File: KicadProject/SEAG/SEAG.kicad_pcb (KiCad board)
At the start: 4 copper layers, 99.1 x 66.1 mm, 82 parts, among them J1 Screw_Terminal_01x02, J11 Screw_Terminal_01x02, J12 Screw_Terminal_01x02, J14 Screw_Terminal_01x08, J2 Conn_01x06_Pin, J3 Screw_Terminal_01x08, J4 Screw_Terminal_01x06, J5 Screw_Terminal_01x06, J6 Screw_Terminal_01x06, J7 Screw_Terminal_01x06, U1 STM32F722RCTx, Y1 Crystal_GND24

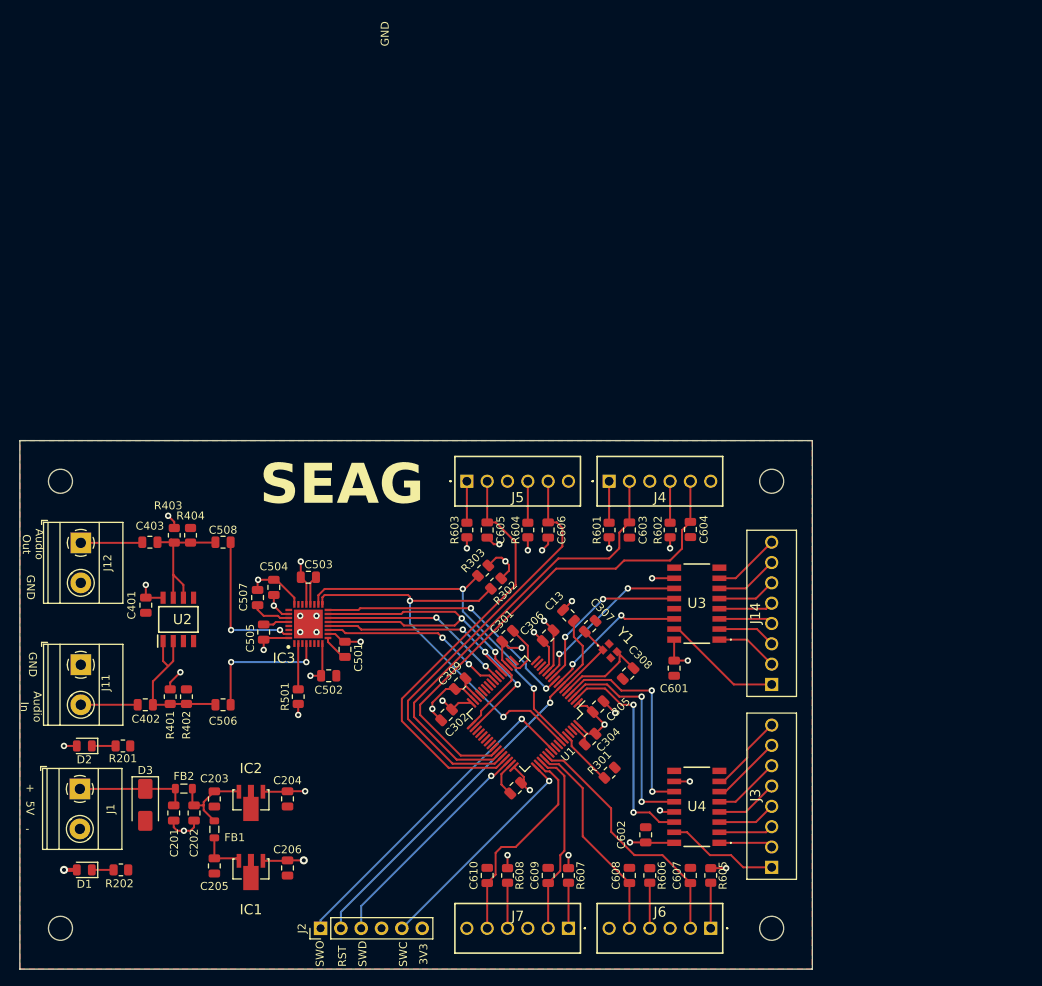
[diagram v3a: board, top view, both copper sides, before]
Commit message: Added rotary encoder screw terminal
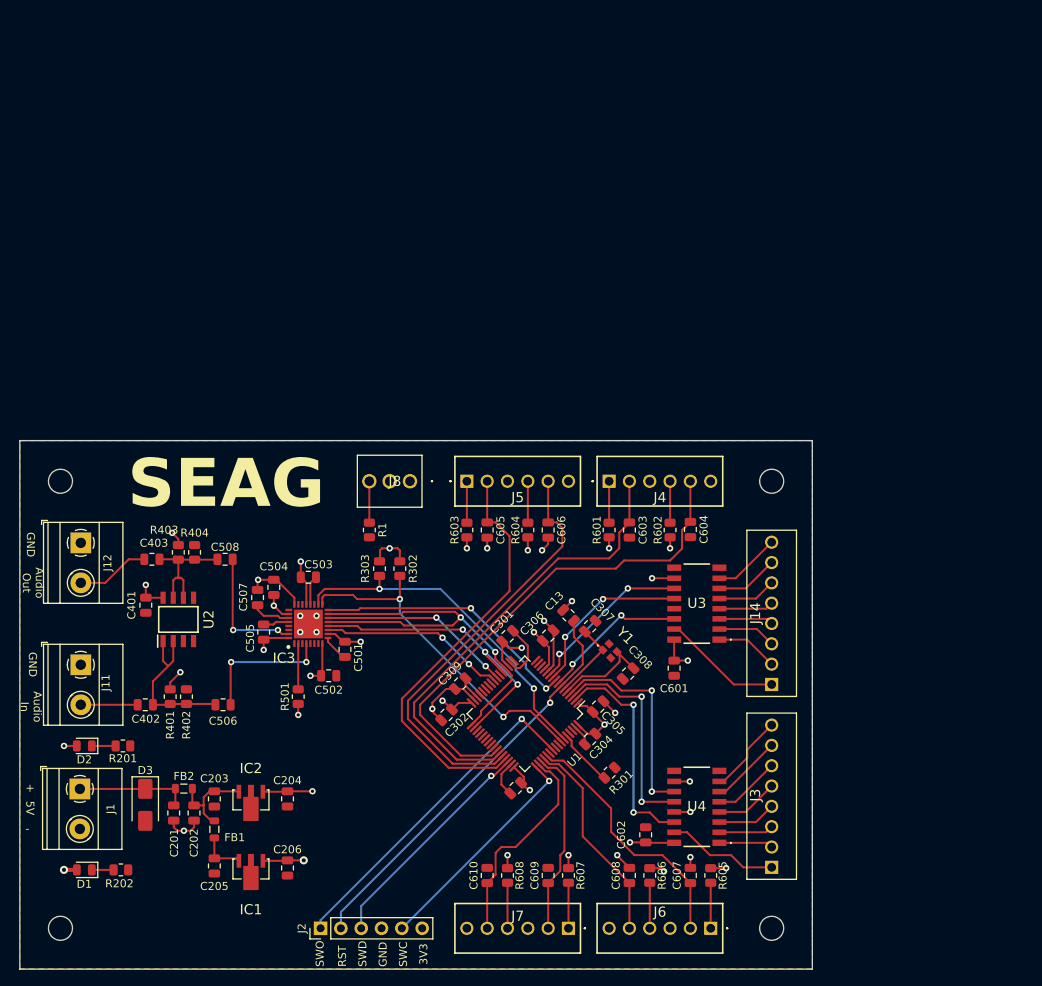
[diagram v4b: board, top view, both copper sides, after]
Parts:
- added J8: Screw_Terminal_01x03, SamacSys_Parts:2828343, F.Cu at (99.6, 91.4)
- added R1: 10K, Resistor_SMD:R_0805_2012Metric, F.Cu at (94.5, 97.5)
- moved R303 13.0 mm to (95.8, 102.4), turned to -90 degrees
- moved R302 12.2 mm to (98.3, 102.4), turned to -90 degrees
- moved R404 2.20 mm to (72.6, 100.3)
- moved R403 2.20 mm to (70.6, 100.3)
- moved C403 2.15 mm to (67.3, 101.2)
- moved C508 2.15 mm to (76.5, 101.2)
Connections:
- C403 pad 2: Net-(J12-Pin_1) -> Net-(J12-Pin_2)
- J12 pad 1: Net-(J12-Pin_1) -> GND
- J12 pad 2: GND -> Net-(J12-Pin_2)
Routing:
- net Net-(J12-Pin_2): track 0.00 -> 9.16 mm
- net I2C.SCL: track 52.1 -> 43.3 mm
- net Net-(J12-Pin_1): track 7.72 -> 0.00 mm
- net Net-(J8-Pin_3): track 0.00 -> 5.29 mm
- net GND: track 62.0 -> 65.2 mm, vias 12 -> 14
- net +3V3: track 73.0 -> 75.8 mm, vias 21 -> 22
- net I2C.SDA: track 46.1 -> 43.5 mm
- net Net-(IC3-HP_L): track 18.4 -> 16.0 mm
- net AudioOut: track 18.2 -> 16.0 mm
- net +3.3VA: track 175.4 -> 173.8 mm
- net ToggleInput3: track 53.8 -> 53.2 mm
- net Net-(IC2-IN): track 11.3 -> 11.9 mm

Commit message: gezevert aan pcb
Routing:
- net GND: track 65.2 -> 71.3 mm, vias 14 -> 16
- net unconnected-(U1-PB14-Pad35): track 0.00 -> 0.84 mm

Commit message: Slight PCB changes
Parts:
- removed R1: 10K, Resistor_SMD:R_0805_2012Metric
- added C311: 1u, Capacitor_SMD:C_0805_2012Metric, F.Cu at (102.4, 121.2)
- moved H1 55.9 mm to (55.9, 147.3)
- moved H2 55.9 mm to (55.9, 91.4)
- moved H3 55.9 mm to (144.8, 147.3)
- moved H4 55.9 mm to (144.8, 91.4)
- moved D2 18.2 mm to (58.5, 142.7)
- moved R201 18.2 mm to (63.3, 142.7)
- moved C302 1.05 mm to (103.9, 119.6), turned to 135 degrees
- moved D1 0.88 mm to (58.6, 139.2)
- moved R202 0.88 mm to (63.1, 139.2)
- renumbered C13 to C310
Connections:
- J8 pad 1: GND -> RotEncoderButton
- J8 pad 2: PotInput -> RotEncoderIn2
- J8 pad 3: Net-(J8-Pin_3) -> RotEncoderIn1
- U1 pad 37: unconnected-(U1-PC6-Pad37) -> RotEncoderIn1
- U1 pad 38: unconnected-(U1-PC7-Pad38) -> RotEncoderIn2
- U1 pad 39: unconnected-(U1-PC8-Pad39) -> RotEncoderButton
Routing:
- net RotEncoderIn2: track 0.00 -> 42.6 mm, vias 0 -> 1
- net RotEncoderIn1: track 0.00 -> 41.8 mm, vias 0 -> 1
- net RotEncoderButton: track 0.00 -> 41.5 mm, vias 0 -> 1
- net Net-(J8-Pin_3): track 5.29 -> 0.00 mm
- net ToggleInput3: track 53.2 -> 56.9 mm
- net ToggleInput4: track 53.6 -> 57.0 mm
- net +3V3: track 75.8 -> 78.9 mm
- net ToggleInput1: track 57.6 -> 60.6 mm
- net +3.3VA: track 173.8 -> 176.4 mm
- net ToggleInput2: track 63.0 -> 65.6 mm
- net unconnected-(U1-PB14-Pad35): track 0.84 -> 0.00 mm
- net GND: track 71.3 -> 71.8 mm

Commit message: Added header
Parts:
- added J9: Conn_01x06_Pin, Connector_PinHeader_2.54mm:PinHeader_1x06_P2.54mm_Vertical, F.Cu at (91.0, 121.5)
- added R609: 10K, Resistor_SMD:R_0805_2012Metric, F.Cu at (97.2, 97.0)
- moved J1 0.63 mm to (58.9, 129.9)
- moved J12 0.51 mm to (58.9, 99.1)
- moved J11 0.46 mm to (58.9, 114.4)
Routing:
- net I2S.WS: track 52.3 -> 85.4 mm, vias 2 -> 4
- net I2S.ASD: track 33.6 -> 62.8 mm, vias 2 -> 4
- net I2C.SDA: track 43.5 -> 65.0 mm, vias 2 -> 3
- net I2S.DSD: track 24.2 -> 43.0 mm, vias 2 -> 3
- net I2S.CLK: track 37.8 -> 55.3 mm, vias 3 -> 4
- net I2C.SCL: track 43.3 -> 58.6 mm, vias 2 -> 3
- net +3V3: track 78.9 -> 83.9 mm
- net RotEncoderButton: track 41.5 -> 43.5 mm, vias 1 -> 2
- net Net-(D3-A1): track 14.5 -> 13.9 mm
- net Net-(J12-Pin_2): track 9.16 -> 8.65 mm
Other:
- board text added: "C SCL"
- board text added: "C SDA"
- board text added: "S ASD"
- board text added: "S CLK"
- board text added: "S DSD"
- board text added: "S WS"
